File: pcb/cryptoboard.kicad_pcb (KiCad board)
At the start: 2 copper layers, 53.3 x 50.8 mm, 36 parts, among them J1 USB_A, J2 BOOT, J3 SWD, J4 USR_LEFT, J5 USR_RIGHT, J6 Conn_01x04, SW1 SW_Push, U2 LM317_SOT-223-3.3V, U3 STM32F107RBTx, Y1 Crystal

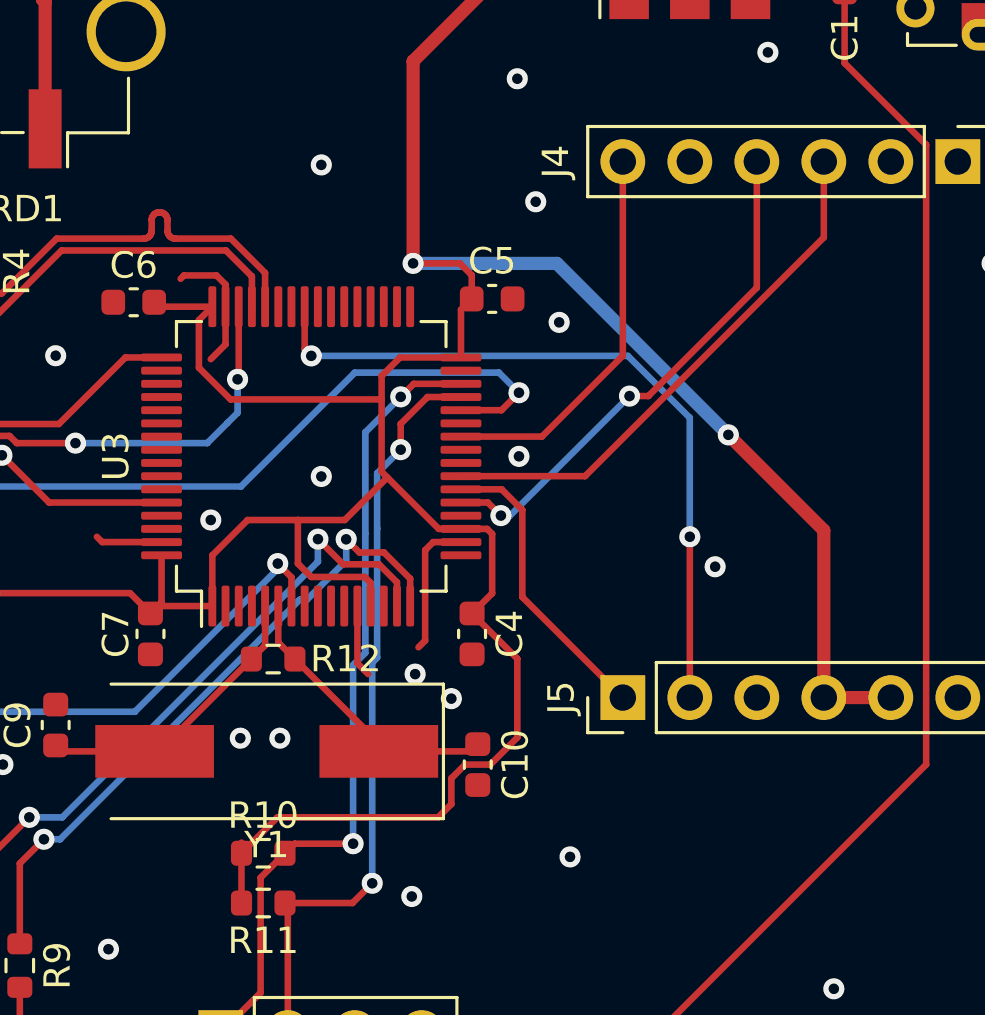
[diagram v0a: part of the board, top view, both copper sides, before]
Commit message: update wiring
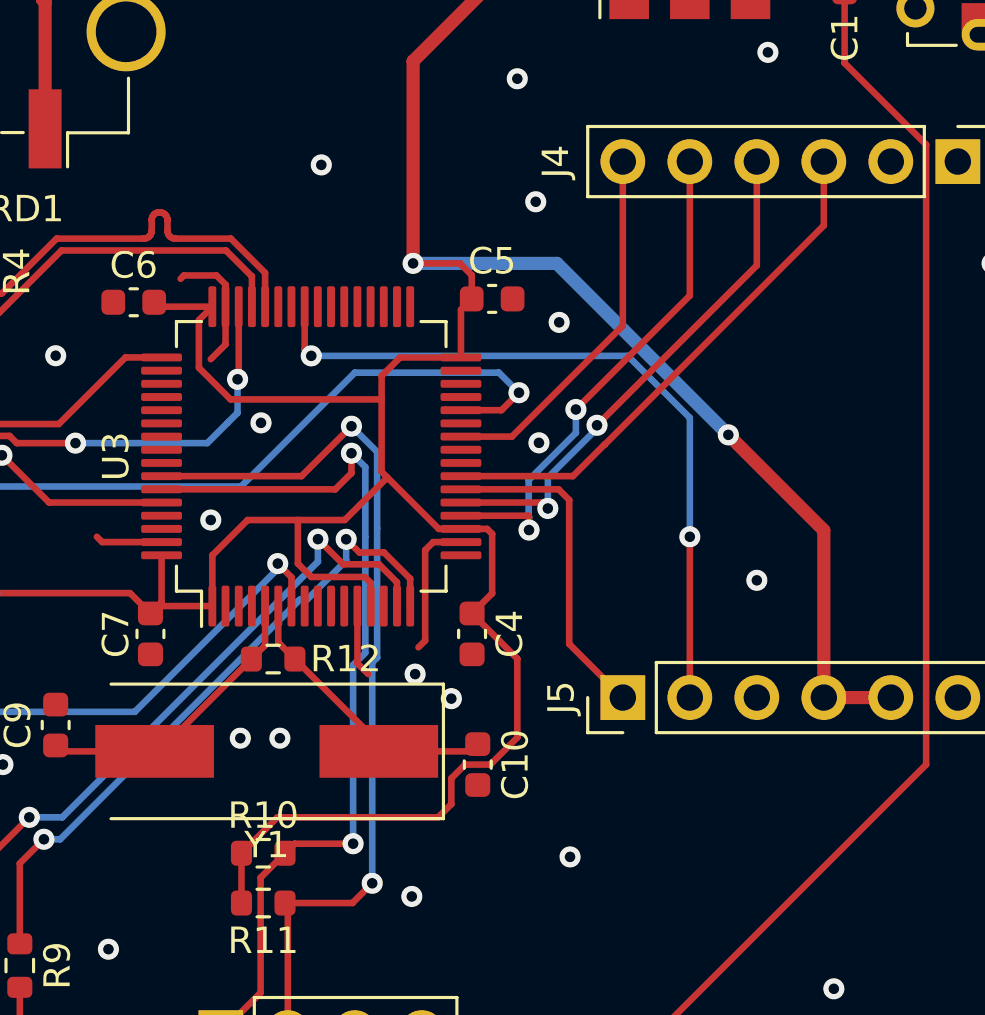
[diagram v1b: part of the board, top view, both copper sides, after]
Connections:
- U3 pad 20: unconnected-(U3-PA4-Pad20) -> SCN
- U3 pad 29: SCL -> unconnected-(U3-PB10-Pad29)
- U3 pad 30: SDA -> unconnected-(U3-PB11-Pad30)
- U3 pad 58: unconnected-(U3-PB6-Pad58) -> SCL
- U3 pad 59: unconnected-(U3-PB7-Pad59) -> SDA
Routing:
- net SCN: track 0.00 -> 19.6 mm, vias 0 -> 2
- net SCL: track 29.1 -> 34.4 mm
- net SDA: track 30.7 -> 34.0 mm
- net MISO: track 11.3 -> 12.6 mm
- net INT: track 14.8 -> 14.1 mm
